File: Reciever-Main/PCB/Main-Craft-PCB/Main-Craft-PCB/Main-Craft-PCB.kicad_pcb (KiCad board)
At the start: 2 copper layers, 68.6 x 99.1 mm, 123 parts, among them J1 nRF24L01_Conn, J10 L298N, J2 IR_SENSOR_1, J3 IR_SENSOR_2, J4 IR_SENSOR_?, J5 IR_SENSOR_?, J6 ESC_1, J7 ESC_2, J8 ESC_3, J9 ESC_4, Q1 2N2219, Q10 2N2219, Q11 2N2219, Q12 2N2219, Q13 2N2219, Q14 2N2219, Q2 2N2219, Q3 2N2219, Q4 2N2219, Q5 2N2219, Q6 2N2219, Q7 2N2219, Q8 2N2219, Q9 2N2219, SW1 SW_Push, SW2 SW_Push, SW3 SW_SPDT, SW4 SW_SPDT, SW5 SW_SPDT, SW6 SW_SPDT, SW7 SW_SPDT, U1 NUCLEO144-F429ZI, U2 LM358DR2G, U3 LM2940-3.0, U4 LM2940-5.0, U5 LM2940-12.0

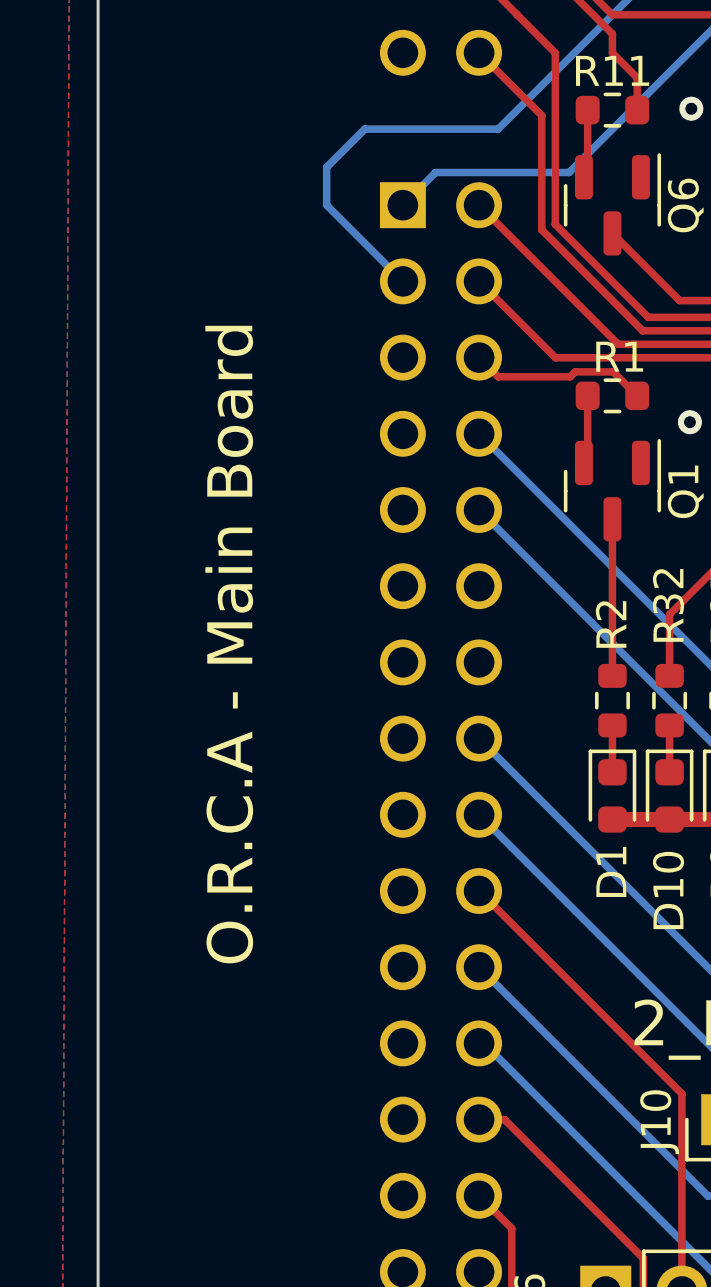
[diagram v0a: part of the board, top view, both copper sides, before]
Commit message: Update Silk Screen
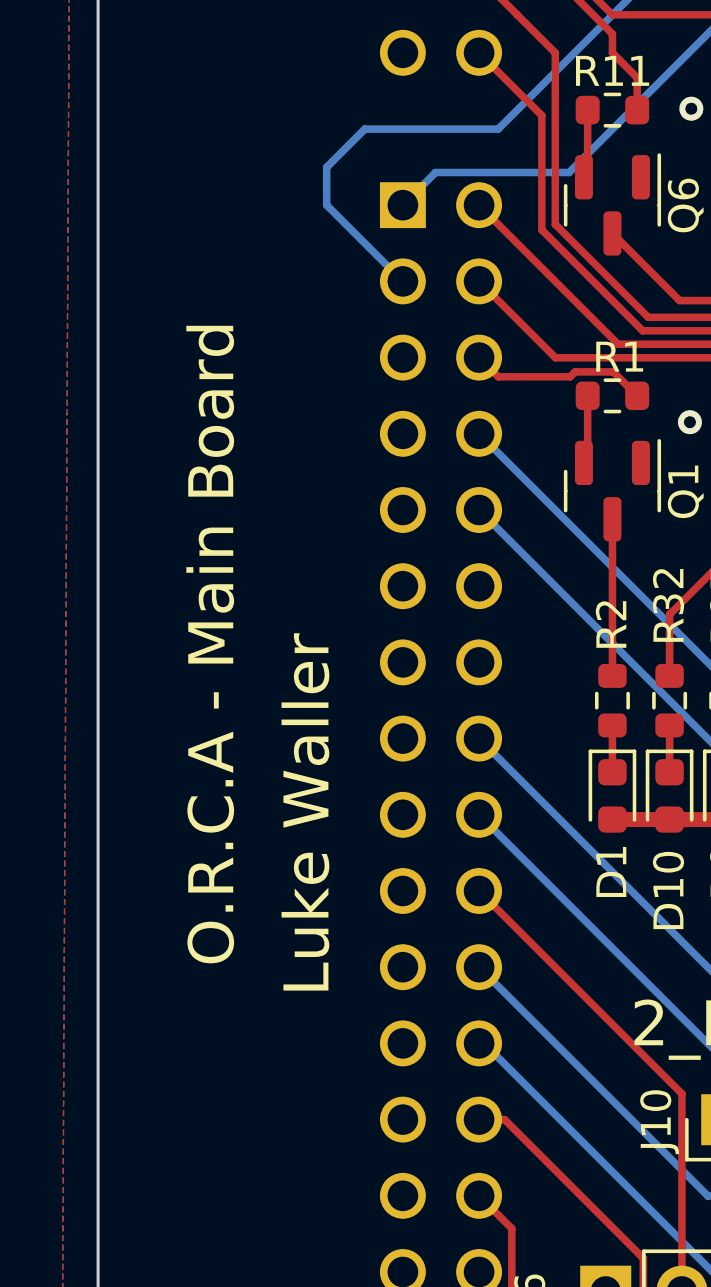
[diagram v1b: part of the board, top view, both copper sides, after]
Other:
- board text added: "Luke Waller"
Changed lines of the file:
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@@
     (effects (font (size 1.5 1.5) (thickness 0.3)))
   )
-  (gr_text "O.R.C.A - Main Board" (at 125.095 111.76 90) (layer "F.SilkS")
+  (gr_text "O.R.C.A - Main Board" (at 124.46 111.76 90) (layer "F.SilkS")
     (effects (font (size 1.5 1.5) (thickness 0.3)))
   )
@@
     (effects (font (size 1.5 1.5) (thickness 0.3)))
   )
+  (gr_text "Luke Waller" (at 127.635 117.475 90) (layer "F.SilkS")
+    (effects (font (size 1.5 1.5) (thickness 0.3)))
+  )
